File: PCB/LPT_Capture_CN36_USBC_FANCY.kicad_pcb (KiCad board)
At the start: 2 copper layers, 68 x 31.7 mm, 26 parts, among them J1 GSB1C411101DS1HR, J2 112-036-213R001, Q1 SL2301S, Q2 SL2301S, U1 FT245RL

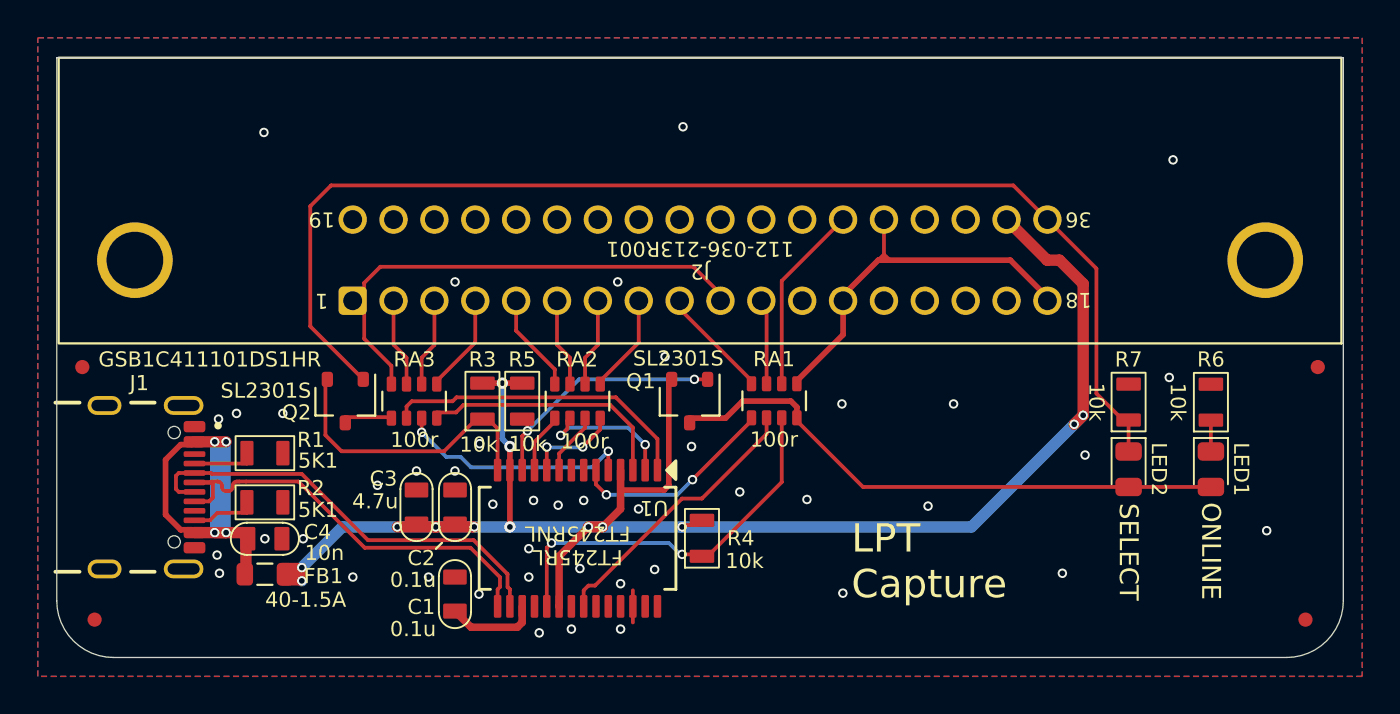
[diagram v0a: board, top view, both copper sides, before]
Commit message: rename Centronics to CN36
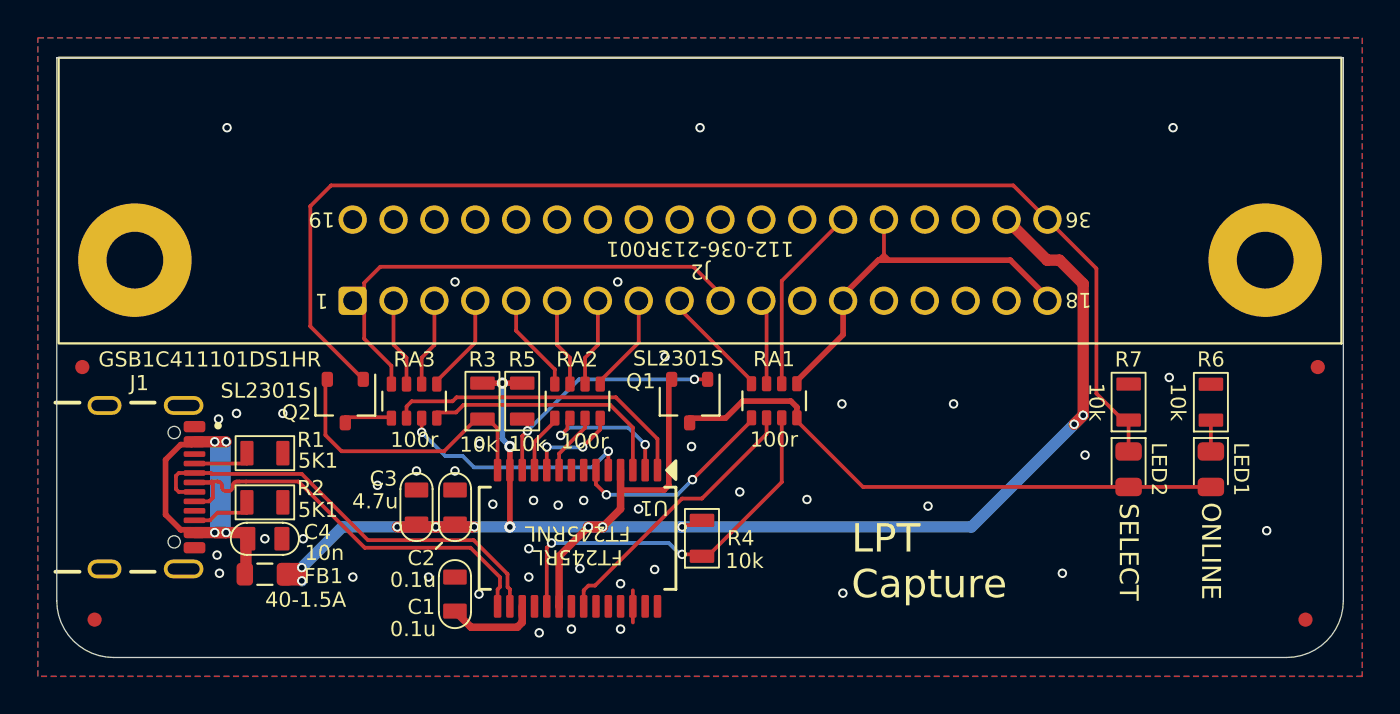
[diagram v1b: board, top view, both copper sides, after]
